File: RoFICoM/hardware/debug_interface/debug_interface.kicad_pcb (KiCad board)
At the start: 2 copper layers, 76.2 x 36.8 mm, 5 parts, among them J1 ST-Link A, J2 UART, J3 ST-Link B, J4 RoFICoM, J5 ST-Link

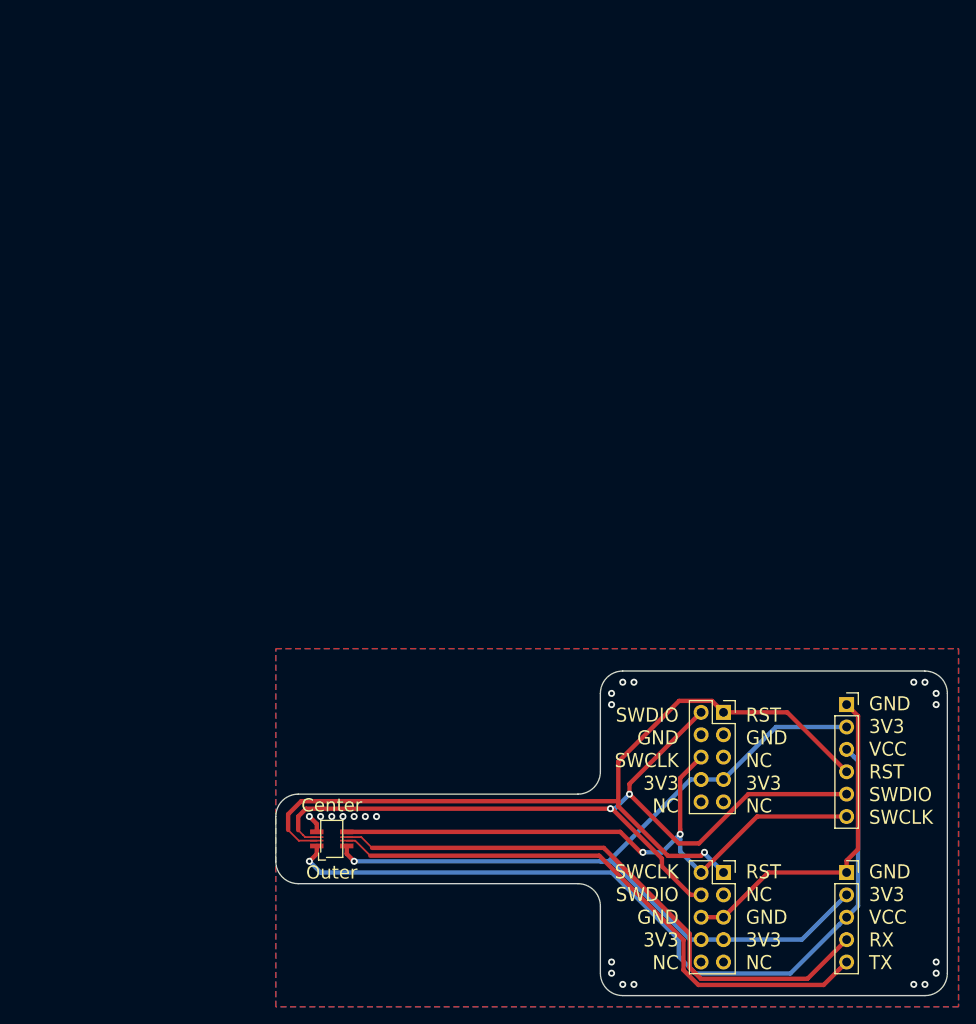
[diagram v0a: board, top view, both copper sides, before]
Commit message: RoFICoM: Rework debug interface into v0.2
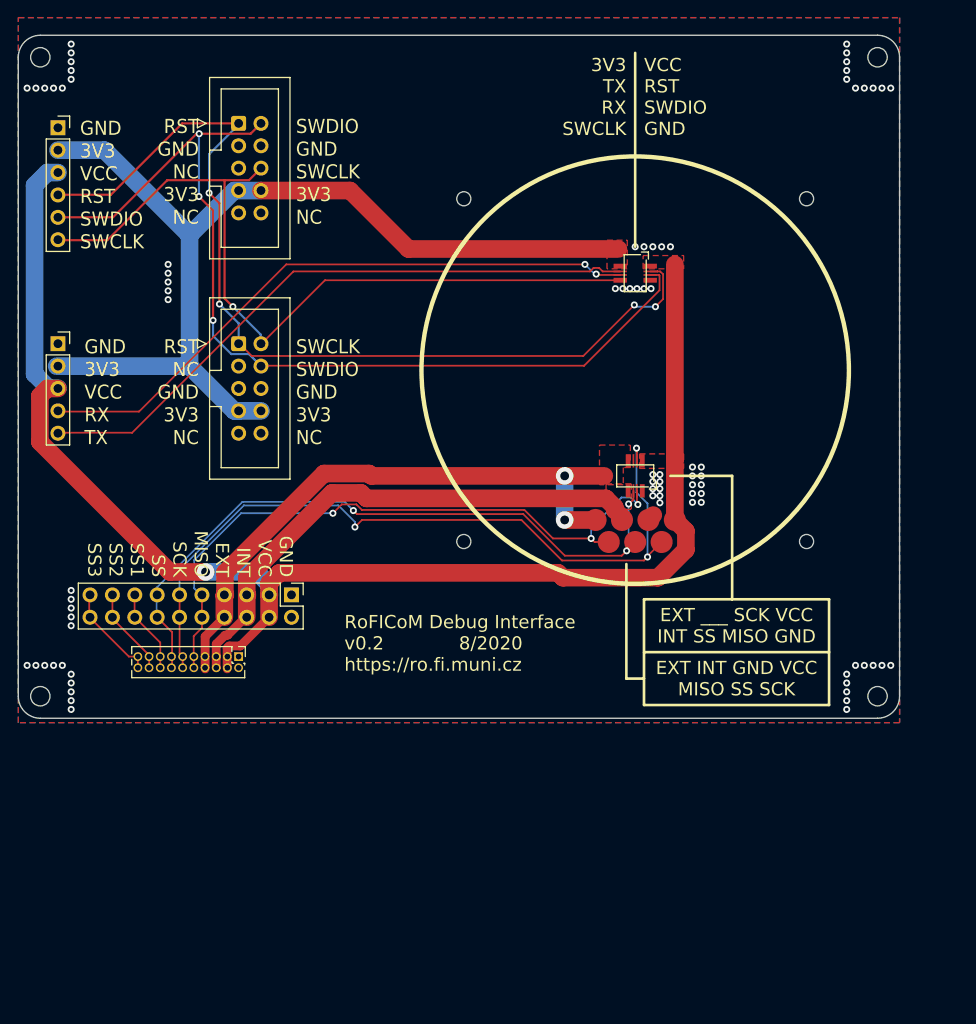
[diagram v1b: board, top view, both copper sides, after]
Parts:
- added H1: MountingHole, rofi:ThreadedHole-M2, F.Cu at (130.6, 89.4)
- added H2: MountingHole, rofi:ThreadedHole-M2, F.Cu at (130.6, 50.6)
- added H3: MountingHole, rofi:ThreadedHole-M2, F.Cu at (169.4, 50.6)
- added H4: MountingHole, rofi:ThreadedHole-M2, F.Cu at (169.4, 89.4)
- added H5: MountingHole, MountingHole:MountingHole_2.2mm_M2, F.Cu at (82.5, 34.5)
- added H6: MountingHole, MountingHole:MountingHole_2.2mm_M2, F.Cu at (82.5, 107.0)
- added H7: MountingHole, MountingHole:MountingHole_2.2mm_M2, F.Cu at (177.5, 34.5)
- added H8: MountingHole, MountingHole:MountingHole_2.2mm_M2, F.Cu at (177.5, 107.0)
- added J6: RoFICoM, rofi:molex-505004-0812, F.Cu at (150.0, 82.0)
- added J7: system-2.54, Connector_PinHeader_2.54mm:PinHeader_2x10_P2.54mm_Vertical, F.Cu at (111.0, 95.5)
- added J8: system-1.27, Connector_PinHeader_1.27mm:PinHeader_2x10_P1.27mm_Vertical, F.Cu at (105.0, 102.5)
- added J9: Conn_01x07, rofi:pogo_pads_4_3, F.Cu at (150.0, 87.0)
- J1, J3: footprint Connector_PinSocket_2.54mm:PinSocket_2x05_P2.54mm_Vertical -> Connector_IDC:IDC-Header_2x05_P2.54mm_Vertical
- J4: value RoFICoM -> RoFICoM-debug
- moved J5 110.9 mm to (84.5, 42.5)
- moved J2 107.7 mm to (84.5, 67.0)
- moved J3 86.6 mm to (105.0, 42.0)
- moved J1 81.4 mm to (105.0, 67.0)
- moved J4 72.8 mm to (150.0, 59.0), turned to 270 degrees
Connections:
- J1 pad 10: Net-(J1-Pad10) -> (no net)
- J1 pad 3: Net-(J1-Pad3) -> (no net)
- J1 pad 9: Net-(J1-Pad9) -> (no net)
- J3 pad 10: Net-(J3-Pad10) -> (no net)
- J3 pad 5: Net-(J3-Pad5) -> (no net)
- J3 pad 9: Net-(J3-Pad9) -> (no net)
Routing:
- net SCK: track 0.00 -> 88.3 mm, vias 0 -> 3
- net SS: track 0.00 -> 78.7 mm, vias 0 -> 3
- net MISO: track 0.00 -> 74.6 mm, vias 0 -> 3
- net VCC: track 92.2 -> 164.2 mm
- net EXT: track 0.00 -> 68.2 mm, vias 0 -> 2
- net INT: track 0.00 -> 60.2 mm
- net GND: track 40.8 -> 0.79 mm, vias 23 -> 80
- net SWCLK: track 73.8 -> 90.7 mm, vias 2 -> 1
- net +3V3: track 98.0 -> 112.6 mm, vias 1 -> 0
- net RST: track 96.3 -> 107.7 mm, vias 1 -> 4
- net SS3: track 0.00 -> 11.3 mm
- net SS2: track 0.00 -> 10.1 mm
- net SWDIO: track 99.4 -> 109.4 mm, vias 2 -> 3
- net SS1: track 0.00 -> 9.53 mm
- net TX: track 66.6 -> 71.9 mm
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- added copper zone on F.Cu, net +3V3
- added copper zone on F.Cu, net EXT
- added copper zone on F.Cu, net INT
- added copper zone on F.Cu, net VCC
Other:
- board size 76.2 x 36.8 mm -> 100 x 77.5 mm
- board text added: "3V3 TX RX SWCLK"
- board text added: "EXT INT GND VCC MISO SS SCK"
- board text added: "EXT ___ SCK VCC INT SS MISO GND"
- board text added: "GND VCC INT EXT MISO SCK SS SS1 SS2 SS3"
- board text added: "RoFICoM Debug Interface v0.2 8/2020 https://ro.fi.muni.cz"
- board text added: "VCC RST SWDIO GND"
- board text removed: "Center"
- board text removed: "Outer"
- board text removed: "RoFICoM Debug Interface v0.1 9/2019 https://ro.fi.muni.cz"
